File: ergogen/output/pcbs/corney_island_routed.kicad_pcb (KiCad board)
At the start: 2 copper layers, 134 x 92.5 mm, 46 parts

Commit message: Update outputs with additional plate files
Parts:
- D1, D10, D11, D12, D13, D14, D15, D16, D17, D18, D19, D2, D20, D21, D3, D4, D5, D6, D7, D8, D9: footprint SmdDiode -> ComboDiode
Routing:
- net R1: track 169.1 -> 137.7 mm, vias 8 -> 7
- net GND: track 81.0 -> 102.5 mm, vias 3 -> 6
- net C1: track 224.1 -> 207.8 mm, vias 4 -> 5
- net C3: track 243.0 -> 227.4 mm
- net R2: track 164.4 -> 154.2 mm, vias 8 -> 10
- net C2: track 188.2 -> 198.4 mm
- net SCL: track 45.1 -> 53.7 mm, vias 1 -> 2
- net index_bottom: track 31.8 -> 37.4 mm
- net VCC: track 62.1 -> 57.7 mm, vias 2 -> 1
- net ring_home: track 29.5 -> 33.8 mm
- net data: track 64.8 -> 69.0 mm, vias 1 -> 3
- net C5: track 174.1 -> 177.5 mm
- net index_home: track 31.8 -> 28.5 mm
- net C0: track 223.3 -> 220.1 mm
- net ring_top: track 31.4 -> 34.0 mm
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
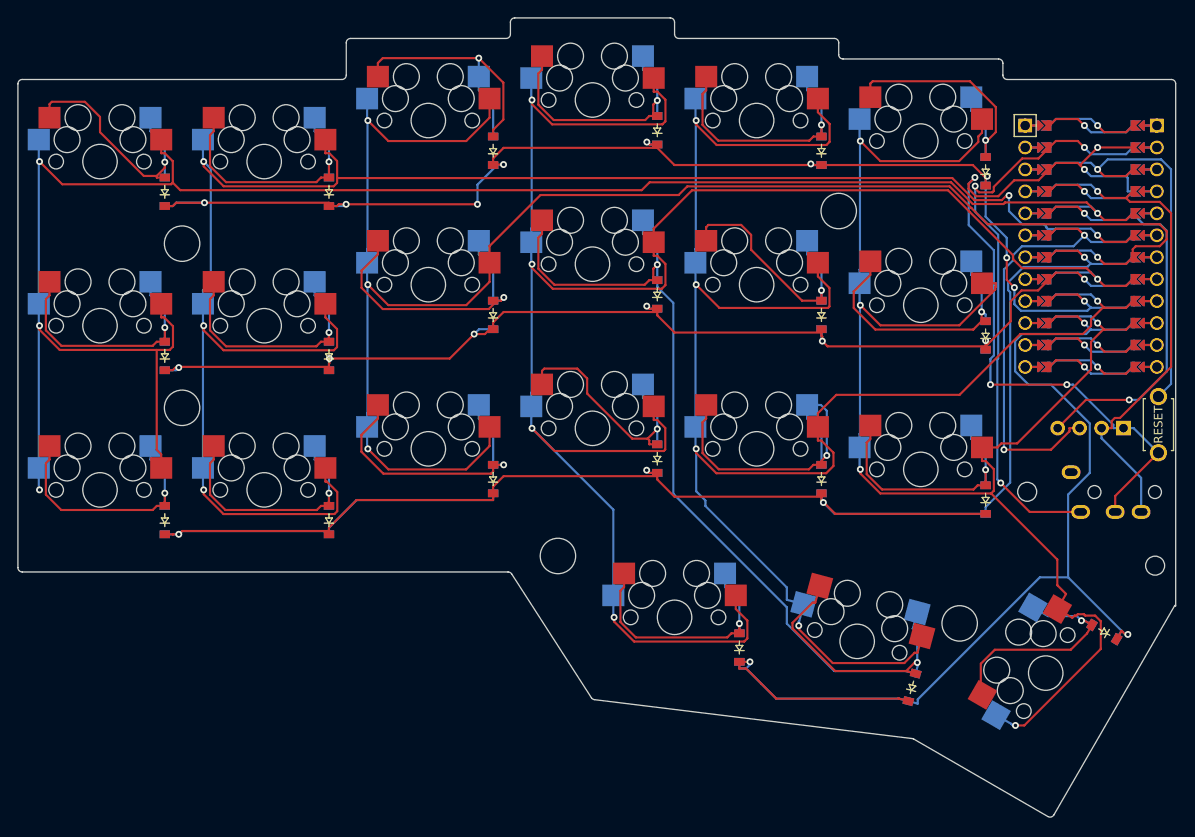
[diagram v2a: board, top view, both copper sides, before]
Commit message: Add LED cutouts
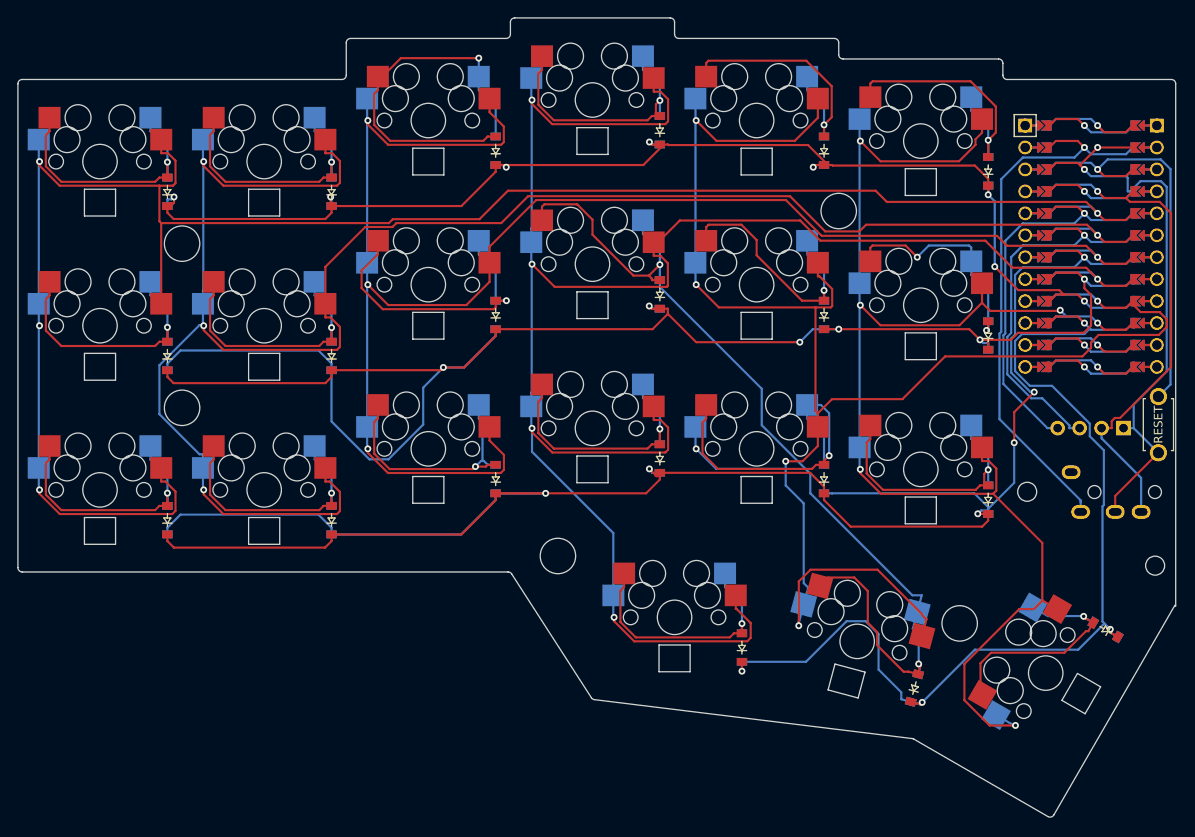
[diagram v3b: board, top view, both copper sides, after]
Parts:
- moved D21 0.30 mm to (216.4, 116.2)
- moved D10 0.30 mm to (164.8, 96.4)
- moved D11 0.30 mm to (164.8, 77.4)
- moved D12 0.30 mm to (164.8, 58.4)
- moved D13 0.30 mm to (183.8, 98.8)
- moved D14 0.30 mm to (183.8, 79.8)
- moved D15 0.30 mm to (183.8, 60.8)
- moved D16 0.30 mm to (202.8, 101.1)
- moved D17 0.30 mm to (202.8, 82.1)
- moved D18 0.30 mm to (202.8, 63.1)
- moved D19 0.30 mm to (174.3, 118.2)
- moved D7 0.30 mm to (145.8, 98.8)
- moved D8 0.30 mm to (145.8, 79.8)
- moved D9 0.30 mm to (145.8, 60.8)
- moved D1 0.30 mm to (107.8, 103.5)
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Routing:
- net R1: track 137.7 -> 199.3 mm, vias 7 -> 6
- net GND: track 102.5 -> 81.0 mm, vias 6 -> 3
- net C1: track 207.8 -> 226.2 mm, vias 5 -> 4
- net R3: track 137.8 -> 121.2 mm, vias 3 -> 4
- net middle_home: track 125.1 -> 109.7 mm
- net R0: track 216.3 -> 231.6 mm, vias 4 -> 6
- net C5: track 177.5 -> 165.1 mm, vias 5 -> 6
- net ring_top: track 34.0 -> 43.5 mm
- net SCL: track 53.7 -> 45.9 mm, vias 2 -> 1
- net R2: track 154.2 -> 148.6 mm, vias 10 -> 8
- net inner_home: track 31.7 -> 26.2 mm, vias 1 -> 2
- net C2: track 198.4 -> 193.2 mm
- net data: track 69.0 -> 64.8 mm, vias 3 -> 1
- net ring_bottom: track 33.4 -> 30.3 mm
- net C0: track 220.1 -> 223.1 mm
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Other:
- outline, holes or cut-outs redrawn

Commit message: Fix key positions to exactly match the corne
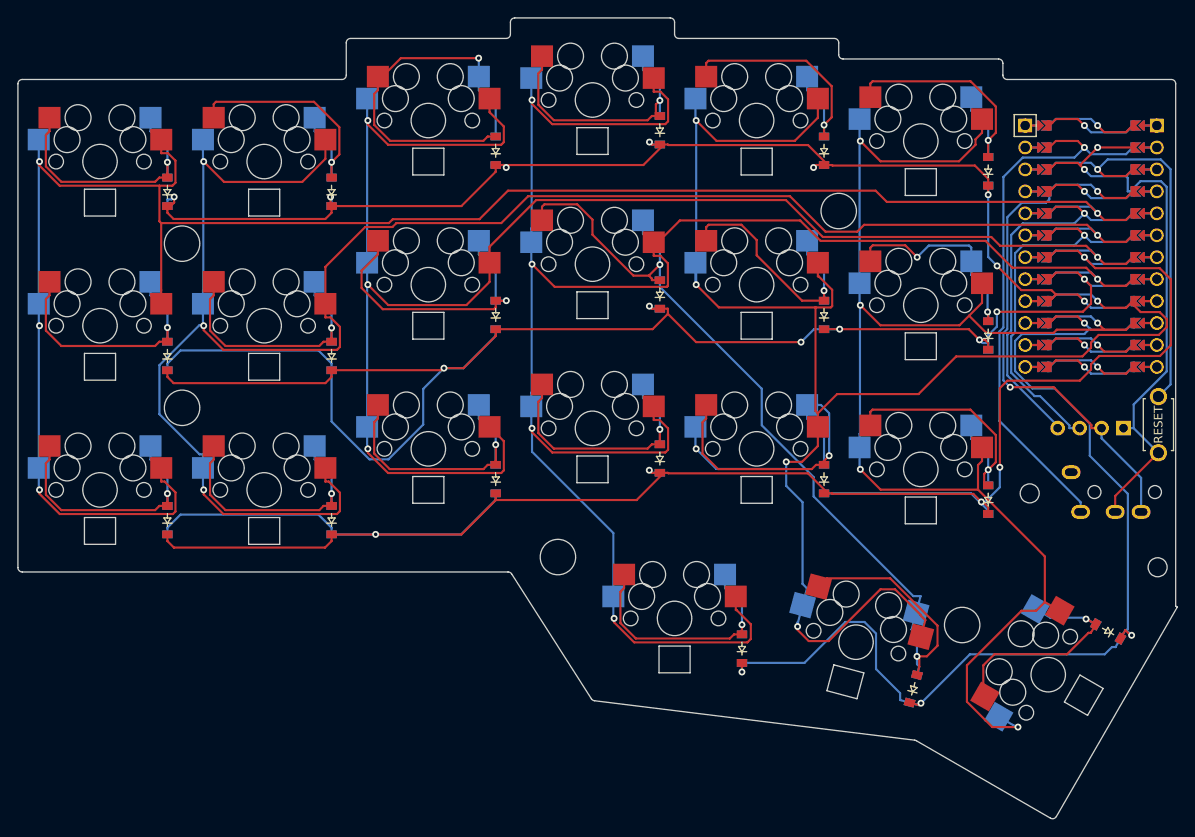
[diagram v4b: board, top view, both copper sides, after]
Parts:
- moved S21 0.34 mm to (209.7, 121.4)
- moved D21 0.34 mm to (216.7, 116.4)
- moved D20 0.16 mm to (194.1, 123.0)
- moved S20 0.16 mm to (187.5, 117.6)
- moved D19 0.12 mm to (174.3, 118.4)
- moved S19 0.12 mm to (166.5, 114.9)
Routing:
- net R0: track 231.6 -> 236.9 mm, vias 6 -> 5
- net C1: track 226.2 -> 221.0 mm
- net VCC: track 57.7 -> 62.1 mm, vias 1 -> 2
- net C5: track 165.1 -> 168.9 mm, vias 6 -> 5
- net R3: track 121.2 -> 124.8 mm
- net middle_home: track 109.7 -> 112.7 mm
- net inner_bottom: track 30.5 -> 32.0 mm
- net inner_home: track 26.2 -> 25.0 mm
- net R2: track 148.6 -> 147.5 mm
- net SDA: track 46.7 -> 45.7 mm
- net C4: track 204.0 -> 203.2 mm
- net pinky_top: track 30.5 -> 31.4 mm
- net ring_bottom: track 30.3 -> 31.1 mm
- net SCL: track 45.9 -> 45.1 mm
- net R1: vias 6 -> 7
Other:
- board size 134 x 92.5 mm -> 134.2 x 92.7 mm

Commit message: Fix screw spacer holes to match the corne
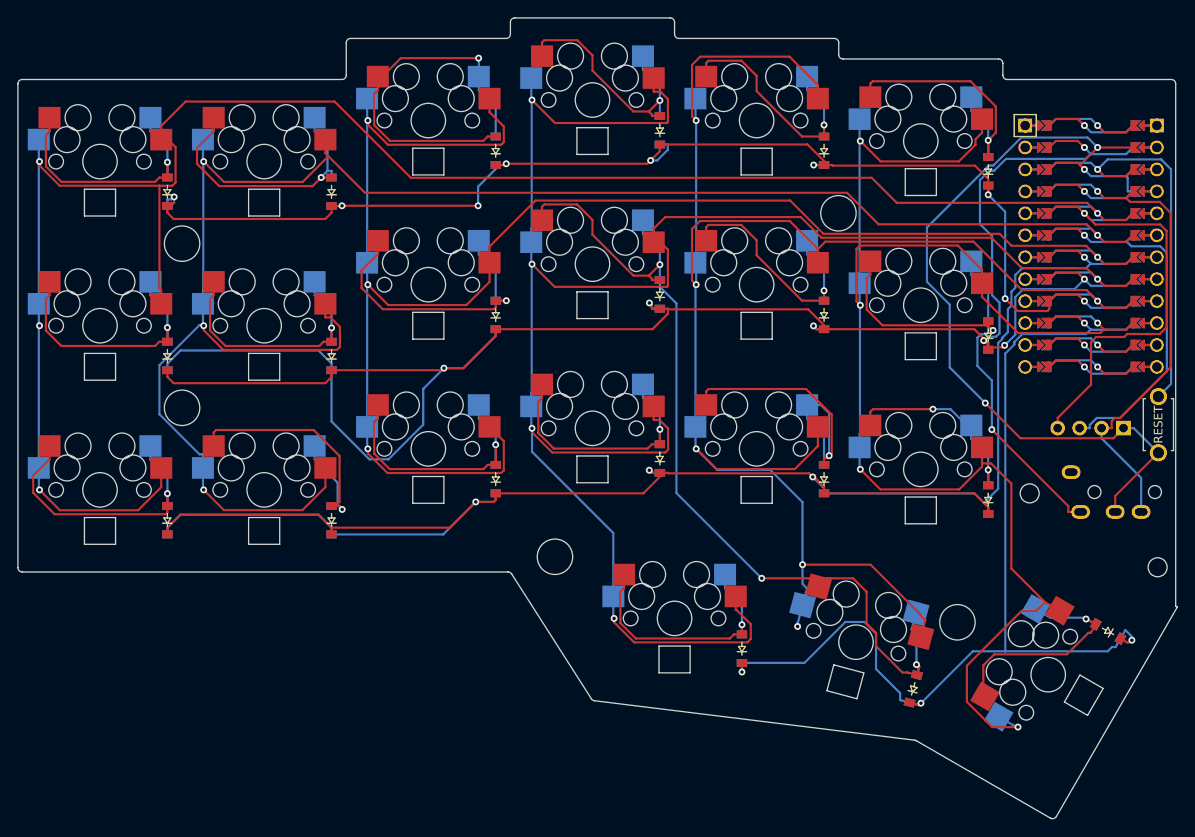
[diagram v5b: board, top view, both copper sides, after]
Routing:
- net GND: track 81.0 -> 112.3 mm, vias 3 -> 4
- net R0: track 236.9 -> 221.5 mm, vias 5 -> 4
- net C1: track 221.0 -> 209.6 mm
- net C5: track 168.9 -> 177.8 mm
- net SDA: track 45.7 -> 54.0 mm
- net inner_bottom: track 32.0 -> 23.9 mm, vias 1 -> 2
- net data: track 64.8 -> 72.9 mm, vias 1 -> 2
- net middle_home: track 112.7 -> 105.4 mm, vias 2 -> 3
- net inner_home: track 25.0 -> 31.3 mm, vias 2 -> 1
- net VCC: track 62.1 -> 57.7 mm, vias 2 -> 1
- net pinky_bottom: track 30.2 -> 34.4 mm
- net R3: track 124.8 -> 120.7 mm
- net R2: track 147.5 -> 150.8 mm, vias 8 -> 9
- net outer_bottom: track 30.2 -> 32.8 mm
- net index_top: track 31.4 -> 29.1 mm
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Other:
- outline, holes or cut-outs redrawn

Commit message: Fix MCU cover mounting holes position
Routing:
- net GND: track 112.3 -> 80.9 mm, vias 4 -> 3
- net SDA: track 54.0 -> 69.6 mm, vias 1 -> 2
- net data: track 72.9 -> 82.8 mm
- net C5: track 177.8 -> 173.2 mm
- net VCC: track 57.7 -> 59.9 mm
- net R1: track 199.2 -> 197.8 mm, vias 6 -> 5
- net R2: track 150.8 -> 151.4 mm
- net SCL: track 43.4 -> 43.5 mm, vias 1 -> 2
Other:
- outline, holes or cut-outs redrawn

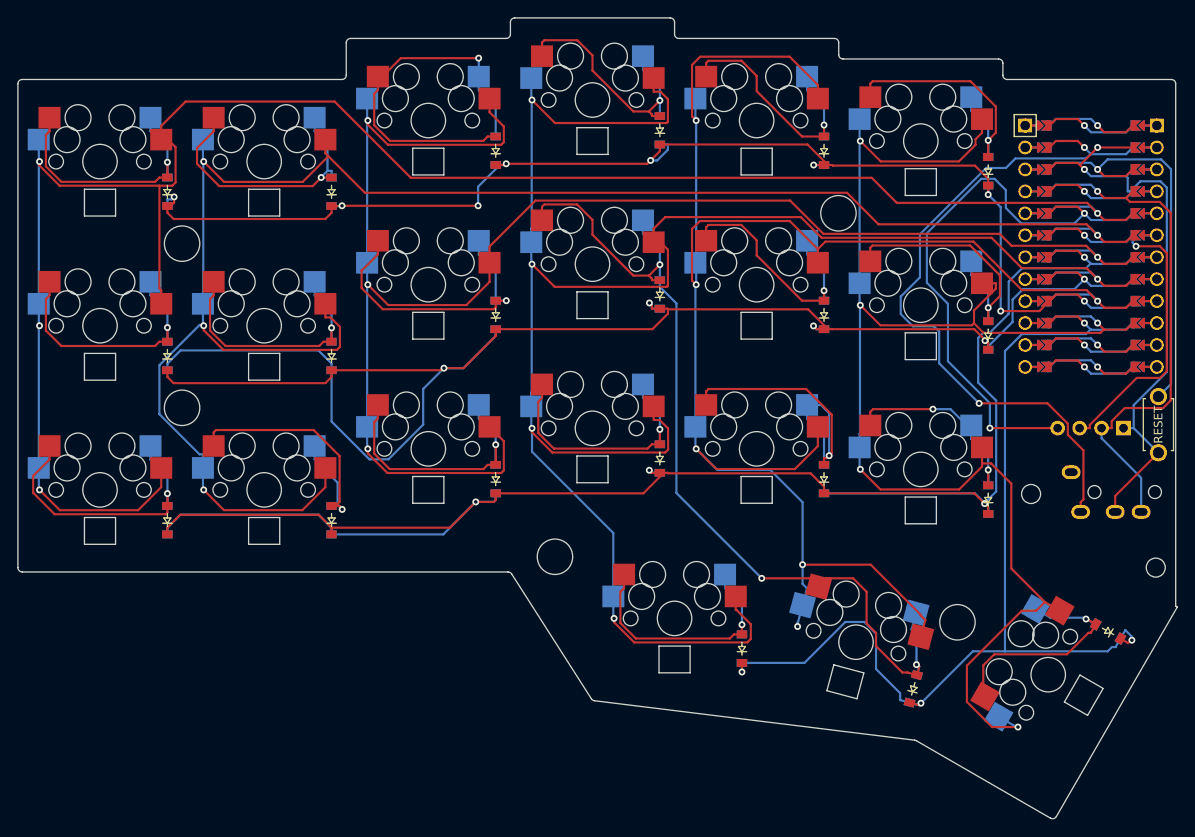
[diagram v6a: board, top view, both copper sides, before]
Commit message: Fix component positions to match the corne
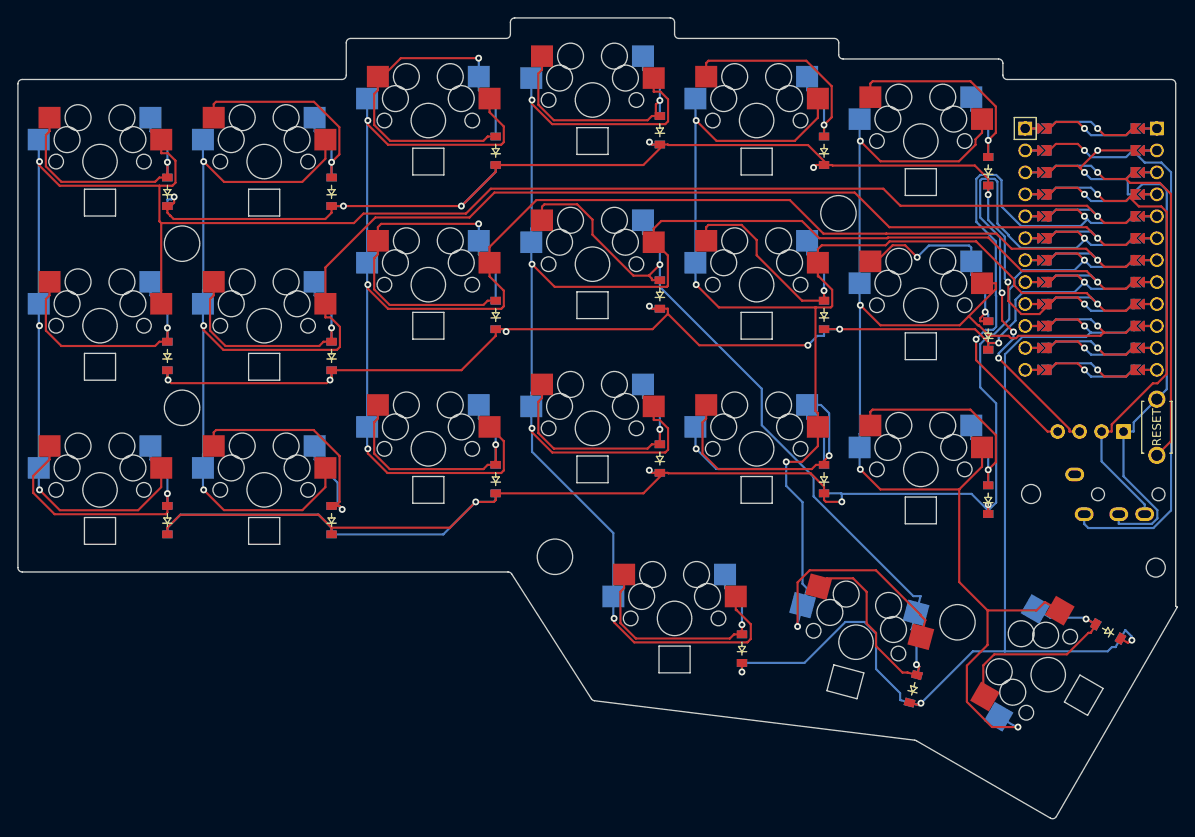
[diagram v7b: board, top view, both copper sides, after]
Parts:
- moved TRRS1 0.49 mm to (224.1, 102.8)
- moved OLED1 0.40 mm to (208.7, 94.8)
- moved B1 0.35 mm to (222.3, 92.8)
- moved MCU1 0.34 mm to (214.7, 72.1)
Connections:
- B1 pad 1: GND -> RST
- B1 pad 2: RST -> GND
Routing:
- net R1: track 197.8 -> 144.2 mm, vias 5 -> 8
- net SCL: track 43.5 -> 66.3 mm, vias 2 -> 4
- net R0: track 221.1 -> 205.6 mm, vias 4 -> 5
- net data: track 82.8 -> 68.0 mm, vias 2 -> 1
- net C4: track 203.2 -> 191.0 mm
- net ring_home: track 33.8 -> 43.9 mm
- net inner_bottom: track 23.9 -> 31.4 mm, vias 2 -> 1
- net inner_home: track 31.7 -> 25.3 mm, vias 1 -> 2
- net C0: track 224.0 -> 218.6 mm
- net C2: track 193.3 -> 198.0 mm
- net SDA: track 69.6 -> 65.1 mm
- net GND: track 80.9 -> 85.4 mm
- net middle_home: track 105.4 -> 109.7 mm, vias 3 -> 2
- net VCC: track 59.9 -> 57.1 mm
- net index_top: track 29.1 -> 31.4 mm
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
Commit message: Update nets and diode positions
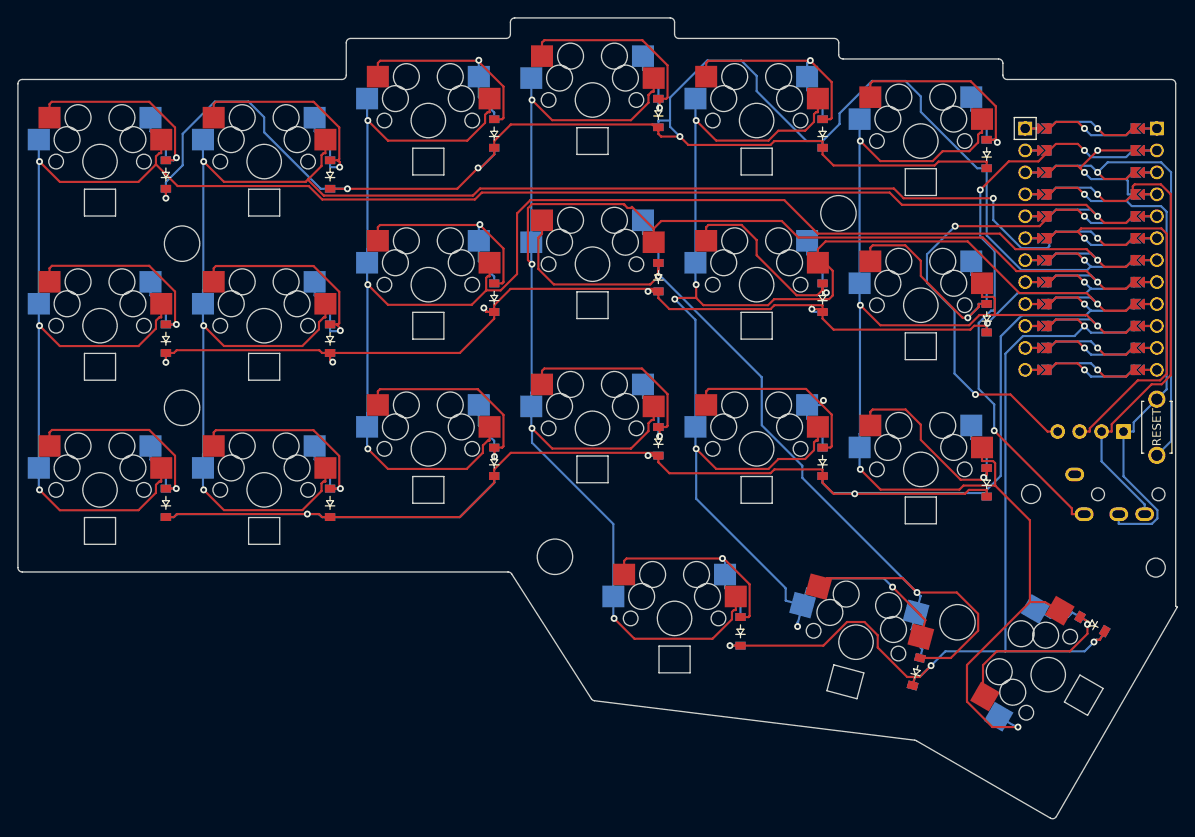
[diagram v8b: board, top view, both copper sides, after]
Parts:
- moved D20 2.01 mm to (194.5, 121.0)
- moved D21 2.01 mm to (214.9, 115.5)
- moved D1 2.01 mm to (107.6, 101.5)
- moved D10 2.01 mm to (164.6, 94.4)
- moved D11 2.01 mm to (164.6, 75.4)
- moved D12 2.01 mm to (164.6, 56.4)
- moved D13 2.01 mm to (183.6, 96.8)
- moved D14 2.01 mm to (183.6, 77.8)
- moved D15 2.01 mm to (183.6, 58.8)
- moved D16 2.01 mm to (202.6, 99.1)
- moved D17 2.01 mm to (202.6, 80.1)
- moved D18 2.01 mm to (202.6, 61.1)
- moved D19 2.01 mm to (174.1, 116.4)
- moved D2 2.01 mm to (107.6, 82.5)
- moved D3 2.01 mm to (107.6, 63.5)
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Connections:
- net P1 renamed LED
- D1 pad 1: R0 -> R2
- D10 pad 1: R0 -> R2
- D12 pad 1: R2 -> R0
- D13 pad 1: R0 -> R2
- D15 pad 1: R2 -> R0
- D16 pad 1: R0 -> R2
- D18 pad 1: R2 -> R0
- D3 pad 1: R2 -> R0
- D4 pad 1: R0 -> R2
- D6 pad 1: R2 -> R0
- D7 pad 1: R0 -> R2
- D9 pad 1: R2 -> R0
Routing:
- net R2: track 153.2 -> 209.9 mm, vias 8 -> 4
- net SCL: track 66.3 -> 51.5 mm, vias 4 -> 1
- net C3: track 226.6 -> 212.1 mm
- net ring_home: track 43.9 -> 30.0 mm
- net ring_top: track 43.5 -> 29.9 mm
- net C1: track 211.2 -> 199.7 mm, vias 4 -> 5
- net R0: track 205.6 -> 216.1 mm
- net C2: track 198.0 -> 189.6 mm
- net middle_home: track 109.7 -> 117.8 mm
- net SDA: track 65.1 -> 57.0 mm, vias 2 -> 3
- net index_bottom: track 37.9 -> 30.6 mm
- net C4: track 191.0 -> 197.9 mm, vias 6 -> 7
- net R3: track 120.4 -> 114.3 mm
- net RST: track 47.7 -> 53.8 mm
- net pinky_bottom: track 34.4 -> 29.3 mm
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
